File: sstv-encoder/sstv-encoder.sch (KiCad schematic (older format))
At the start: 18 parts, among them U1 ANTENNA_CONN, U2 LM386

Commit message: adding new things
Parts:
- added Alt1: AltlMU-10, sstv-encoder:AltIMU-10, symbol project-components:AltlMU-10
- added U3: Adafruit_GPS_MTK3339, sstv-encoder:Adafruit_GPS, symbol project-components:Adafruit_GPS_MTK3339
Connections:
- net +3V3: now also Alt1.5 (VIN), U3.8 (VIN)
- net GNDREF: now also Alt1.3 (GND), U3.7 (GND)
- net TX_GPS: now reaches DUE1.11 (RX3)
- net TX_GPS: now also U3.5 (TX)
- net RX_GPS: now reaches DUE1.12 (TX3)
- net RX_GPS: now also U3.6 (RX)
- net AF_APRS: now reaches DUE1.21 (D2)
- new net SCL_IMU: Alt1.1 (SCL)
- new net SDA_IMU: Alt1.2 (SDA)
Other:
- moved on the sheet: SIN1
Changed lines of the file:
@@
 L project-components:ADS9850 SIN1
 U 1 1 5E6BC8CF
-P 3200 4900
-F 0 "SIN1" H 3050 6515 50  0000 C CNN
-F 1 "ADS9850" H 3050 6424 50  0000 C CNN
-F 2 "sstv-encoder:AD9850" H 3050 4950 50  0001 C CNN
-F 3 "" H 3050 4950 50  0001 C CNN
-	1    3200 4900
-	1    0    0    -1
-$EndComp
-Wire Wire Line
-	2400 3650 1850 3650
-Wire Wire Line
-	1850 3650 1850 3300
+P 2800 5300
+F 0 "SIN1" H 2650 6915 50  0000 C CNN
+F 1 "ADS9850" H 2650 6824 50  0000 C CNN
+F 2 "sstv-encoder:AD9850" H 2650 5350 50  0001 C CNN
+F 3 "" H 2650 5350 50  0001 C CNN
+	1    2800 5300
+	1    0    0    -1
+$EndComp
+Wire Wire Line
+	2000 4050 1450 4050
+Wire Wire Line
+	1450 4050 1450 3700
 $Comp
 L power:+5V #PWR0113
 U 1 1 5E6ECCC4
-P 1850 3300
-F 0 "#PWR0113" H 1850 3150 50  0001 C CNN
-F 1 "+5V" H 1865 3473 50  0000 C CNN
-F 2 "" H 1850 3300 50  0001 C CNN
-F 3 "" H 1850 3300 50  0001 C CNN
-	1    1850 3300
-	1    0    0    -1
-$EndComp
-Wire Wire Line
-	2400 3750 1600 3750
-Wire Wire Line
-	2400 3850 1600 3850
-Wire Wire Line
-	2400 3950 1600 3950
-Wire Wire Line
-	2400 4050 1600 4050
-Wire Wire Line
-	2400 4150 1200 4150
-Wire Wire Line
-	1200 4150 1200 4500
+P 1450 3700
+F 0 "#PWR0113" H 1450 3550 50  0001 C CNN
+F 1 "+5V" H 1465 3873 50  0000 C CNN
+F 2 "" H 1450 3700 50  0001 C CNN
+F 3 "" H 1450 3700 50  0001 C CNN
+	1    1450 3700
+	1    0    0    -1
+$EndComp
+Wire Wire Line
+	2000 4150 1200 4150
+Wire Wire Line
+	2000 4250 1200 4250
+Wire Wire Line
+	2000 4350 1200 4350
+Wire Wire Line
+	2000 4450 1200 4450
+Wire Wire Line
+	2000 4550 800  4550
+Wire Wire Line
+	800  4550 800  4900
 $Comp
 L power:GNDREF #PWR0114
 U 1 1 5E6F3B16
-P 1200 4500
-F 0 "#PWR0114" H 1200 4250 50  0001 C CNN
-F 1 "GNDREF" H 1205 4327 50  0000 C CNN
-F 2 "" H 1200 4500 50  0001 C CNN
-F 3 "" H 1200 4500 50  0001 C CNN
-	1    1200 4500
-	1    0    0    -1
-$EndComp
-Wire Wire Line
-	2400 4550 1650 4550
-Wire Wire Line
-	3700 4550 4250 4550
-Wire Wire Line
-	4250 4550 4250 4950
+P 800 4900
+F 0 "#PWR0114" H 800 4650 50  0001 C CNN
+F 1 "GNDREF" H 805 4727 50  0000 C CNN
+F 2 "" H 800 4900 50  0001 C CNN
+F 3 "" H 800 4900 50  0001 C CNN
+	1    800  4900
+	1    0    0    -1
+$EndComp
+Wire Wire Line
+	2000 4950 1250 4950
+Wire Wire Line
+	3300 4950 3850 4950
+Wire Wire Line
+	3850 4950 3850 5350
 $Comp
 L power:GNDREF #PWR0115
 U 1 1 5E6F749A
-P 4250 4950
-F 0 "#PWR0115" H 4250 4700 50  0001 C CNN
-F 1 "GNDREF" H 4255 4777 50  0000 C CNN
-F 2 "" H 4250 4950 50  0001 C CNN
-F 3 "" H 4250 4950 50  0001 C CNN
-	1    4250 4950
-	1    0    0    -1
-$EndComp
-Text Label 1600 3750 0    50   ~ 0
+P 3850 5350
+F 0 "#PWR0115" H 3850 5100 50  0001 C CNN
+F 1 "GNDREF" H 3855 5177 50  0000 C CNN
+F 2 "" H 3850 5350 50  0001 C CNN
+F 3 "" H 3850 5350 50  0001 C CNN
+	1    3850 5350
+	1    0    0    -1
+$EndComp
+Text Label 1200 4150 0    50   ~ 0
 W_CLK_ADS
-Text Label 1600 3850 0    50   ~ 0
+Text Label 1200 4250 0    50   ~ 0
 FQ_UD_ADS
-Text Label 1600 3950 0    50   ~ 0
+Text Label 1200 4350 0    50   ~ 0
 DATA_ADS
-Text Label 1600 4050 0    50   ~ 0
+Text Label 1200 4450 0    50   ~ 0
 RESET_ADS
 Wire Wire Line
@@
 Text Label 4050 1750 0    50   ~ 0
 RESET_ADS
-Text Label 1650 4550 0    50   ~ 0
+Text Label 1250 4950 0    50   ~ 0
 ZOUT_ADS
 $Comp
@@
 Text Notes 7600 2300 0    50   ~ 0
 50 ohm
+$Comp
+L project-components:Adafruit_GPS_MTK3339 U3
+U 1 1 5E71EA4C
+P 5050 3600
+F 0 "U3" H 5025 4025 50  0000 C CNN
+F 1 "Adafruit_GPS_MTK3339" H 5025 3934 50  0000 C CNN
+F 2 "sstv-encoder:Adafruit_GPS" H 5000 3400 50  0001 C CNN
+F 3 "" H 5000 3400 50  0001 C CNN
+	1    5050 3600
+	1    0    0    -1
+$EndComp
+$Comp
+L project-components:AltlMU-10 Alt1
+U 1 1 5E71F53C
+P 5500 5200
+F 0 "Alt1" H 5475 5775 50  0000 C CNN
+F 1 "AltlMU-10" H 5475 5684 50  0000 C CNN
+F 2 "sstv-encoder:AltIMU-10" H 5500 5200 50  0001 C CNN
+F 3 "" H 5500 5200 50  0001 C CNN
+	1    5500 5200
+	1    0    0    -1
+$EndComp
+$Comp
+L power:GNDREF #PWR01
+U 1 1 5E720A54
+P 4050 4050
+F 0 "#PWR01" H 4050 3800 50  0001 C CNN
+F 1 "GNDREF" H 4055 3877 50  0000 C CNN
+F 2 "" H 4050 4050 50  0001 C CNN
+F 3 "" H 4050 4050 50  0001 C CNN
+	1    4050 4050
+	1    0    0    -1
+$EndComp
+$Comp
+L power:GNDREF #PWR02
+U 1 1 5E72154B
+P 4950 5250
+F 0 "#PWR02" H 4950 5000 50  0001 C CNN
+F 1 "GNDREF" H 4955 5077 50  0000 C CNN
+F 2 "" H 4950 5250 50  0001 C CNN
+F 3 "" H 4950 5250 50  0001 C CNN
+	1    4950 5250
+	1    0    0    -1
+$EndComp
+Wire Wire Line
+	6400 3800 5850 3800
+$Comp
+L power:+3.3V #PWR04
+U 1 1 5E72C5C7
+P 6550 4950
+F 0 "#PWR04" H 6550 4800 50  0001 C CNN
+F 1 "+3.3V" H 6565 5123 50  0000 C CNN
+F 2 "" H 6550 4950 50  0001 C CNN
+F 3 "" H 6550 4950 50  0001 C CNN
+	1    6550 4950
+	1    0    0    -1
+$EndComp
+Wire Wire Line
+	5850 4950 6550 4950
+Wire Wire Line
+	3350 2600 4050 2600
+Wire Wire Line
+	3350 2700 4050 2700
+Wire Wire Line
+	5100 5050 4950 5050
+Wire Wire Line
+	4950 5050 4950 5250
+Wire Wire Line
+	5100 4950 4750 4950
+Wire Wire Line
+	5100 4850 4750 4850
+Text Label 4750 4950 0    50   ~ 0
+SDA_IMU
+Text Label 4750 4850 0    50   ~ 0
+SCL_IMU
+Text Label 4050 2600 0    50   ~ 0
+SDA_IMU
+Text Label 4050 2700 0    50   ~ 0
+SCL_IMU
+Wire Wire Line
+	4050 4050 4050 3800
+Wire Wire Line
+	4050 3800 4200 3800
+Wire Wire Line
+	5850 3400 6400 3400
+Wire Wire Line
+	5850 3500 6400 3500
+Text Label 6400 3400 0    50   ~ 0
+TX_GPS
+Text Label 6400 3500 0    50   ~ 0
+RX_GPS
+Wire Wire Line
+	2300 2600 1700 2600
+Wire Wire Line
+	2300 2700 1700 2700
+Text Label 1700 2600 0    50   ~ 0
+TX_GPS
+Text Label 1700 2700 0    50   ~ 0
+RX_GPS
+$Comp
+L power:+3.3V #PWR03
+U 1 1 5E762D52
+P 6400 3800
+F 0 "#PWR03" H 6400 3650 50  0001 C CNN
+F 1 "+3.3V" H 6415 3973 50  0000 C CNN
+F 2 "" H 6400 3800 50  0001 C CNN
+F 3 "" H 6400 3800 50  0001 C CNN
+	1    6400 3800
+	1    0    0    -1
+$EndComp
+Wire Wire Line
+	3350 2350 4050 2350
+Text Label 4050 2350 0    50   ~ 0
+AF_APRS
 $EndSCHEMATC

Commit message: update sch
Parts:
- added C?: C, symbol Device:C
- added RV?: 10K, Potentiometer_SMD:Potentiometer_Bourns_3214J_Horizontal, symbol Device:R_POT
- added U?: TL082, symbol Amplifier_Operational:TL082
- added U?: 4053, symbol 4xxx:4053
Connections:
- net +5V: now also U?.16 (VDD)
- net AF_APRS: now also C?.2
- net GNDREF: now also RV?.3
- net SCL_IMU: now also DUE1.24 (SCL)
- net SDA_IMU: now also DUE1.23 (SDA)
- net ZOUT_ADS: now also U?.12 (X0); no longer R1.2
- net MUX_SL: now reaches DUE1.22 (D37)
- net MUX_SL: now also U?.11 (A)
- new net: C?.1, RV?.1
- new net: RV?.2, U?.3 (+)
- new net AF_APRS_NORM: U?.1, U?.13 (X1), U?.2 (-)
- new net AF_MUX: R1.2, U?.14 (X)
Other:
- note added: "ANALOG SIGNAL MULTIPLEXOR"
- note added: "AUDIO AMPLIFIER"
- note added: "PWN SIGNAL CORRECTION - APRS"
- moved on the sheet: C5, C7, R1, R2, RV1, U2

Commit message: update schematic
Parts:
- removed U?: 4053, symbol 4xxx:4053
- added C10, C11: 10uF, Capacitor_THT:CP_Radial_D5.0mm_P2.50mm, symbol Device:CP1
- added U5: DG419LDJ, Package_DIP:DIP-8_W7.62mm, symbol Analog_Switch:DG419LDJ
- added U6: LTC1044, Package_DIP:DIP-8_W7.62mm, symbol Regulator_SwitchedCapacitor:LTC1044
- C9: renamed from C?; value C -> 1uF; footprint (none) -> Capacitor_THT:CP_Radial_D5.0mm_P2.50mm
- RV1: footprint Potentiometer_SMD:Potentiometer_Bourns_3214J_Horizontal -> Potentiometer_THT:Potentiometer_Piher_PT-10-V10_Vertical
- RV2: renamed from RV?; footprint Potentiometer_SMD:Potentiometer_Bourns_3214J_Horizontal -> Potentiometer_THT:Potentiometer_Piher_PT-10-V10_Vertical
- U4: renamed from U?; footprint (none) -> Package_DIP:DIP-8-16_W7.62mm
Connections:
- net +3V3: now also U6.8 (V+); no longer U3.8 (VIN)
- net +5V: now also U3.8 (VIN)
- net AF_APRS: now also U5.2
- net AF_MUX: now also U5.1
- net GNDREF: now also C10.1, U6.3 (GND), U6.7 (OSC)
- net MUX_SL: now also U5.6
- net ZOUT_ADS: now also U5.8
- new net: C11.1, U6.2 (CAP+)
- new net: C11.2, U6.4 (CAP-)
- new net -VCC3.3: C10.2, U6.5 (VOUT)
- no-connect marks 0 -> 2
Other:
- note added: "DC-DC INVERTER"
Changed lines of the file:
@@
 F 0 "RV1" H 9381 8896 50  0000 R CNN
 F 1 "10K" H 9381 8805 50  0000 R CNN
-F 2 "Potentiometer_SMD:Potentiometer_Bourns_3214J_Horizontal" H 9450 8850 50  0001 C CNN
+F 2 "Potentiometer_THT:Potentiometer_Piher_PT-10-V10_Vertical" H 9450 8850 50  0001 C CNN
 F 3 "~" H 9450 8850 50  0001 C CNN
 	1    9450 8850
@@
 	1    0    0    -1
 $EndComp
-Text Notes 7600 2300 0    50   ~ 0
+Text Notes 7750 2300 0    50   ~ 0
 50 ohm
 $Comp
@@
 Text Label 1700 2700 0    50   ~ 0
 RX_GPS
-$Comp
-L power:+3.3V #PWR03
-U 1 1 5E762D52
-P 6400 3800
-F 0 "#PWR03" H 6400 3650 50  0001 C CNN
-F 1 "+3.3V" H 6415 3973 50  0000 C CNN
-F 2 "" H 6400 3800 50  0001 C CNN
-F 3 "" H 6400 3800 50  0001 C CNN
-	1    6400 3800
-	1    0    0    -1
-$EndComp
 Wire Wire Line
 	3350 2350 4050 2350
@@
 PWN SIGNAL CORRECTION - APRS
 $Comp
-L Device:C C?
+L Device:C C9
 U 1 1 5E8B30D2
 P 1300 8850
-F 0 "C?" V 1048 8850 50  0000 C CNN
-F 1 "C" V 1139 8850 50  0000 C CNN
-F 2 "" H 1338 8700 50  0001 C CNN
+F 0 "C9" V 1048 8850 50  0000 C CNN
+F 1 "1uF" V 1139 8850 50  0000 C CNN
+F 2 "Capacitor_THT:CP_Radial_D5.0mm_P2.50mm" H 1338 8700 50  0001 C CNN
 F 3 "~" H 1300 8850 50  0001 C CNN
 	1    1300 8850
@@
 $EndComp
 $Comp
-L Amplifier_Operational:TL082 U?
+L Amplifier_Operational:TL082 U4
 U 1 1 5E8B35EC
 P 2600 8950
-F 0 "U?" H 2600 9317 50  0000 C CNN
+F 0 "U4" H 2600 9317 50  0000 C CNN
 F 1 "TL082" H 2600 9226 50  0000 C CNN
-F 2 "" H 2600 8950 50  0001 C CNN
+F 2 "Package_DIP:DIP-8-16_W7.62mm" H 2600 8950 50  0001 C CNN
 F 3 "http://www.ti.com/lit/ds/symlink/tl081.pdf" H 2600 8950 50  0001 C CNN
 	1    2600 8950
@@
 $EndComp
 $Comp
-L Device:R_POT RV?
+L Device:R_POT RV2
 U 1 1 5E8B8628
 P 1650 9150
-F 0 "RV?" H 1581 9196 50  0000 R CNN
+F 0 "RV2" H 1581 9196 50  0000 R CNN
 F 1 "10K" H 1581 9105 50  0000 R CNN
-F 2 "Potentiometer_SMD:Potentiometer_Bourns_3214J_Horizontal" H 1650 9150 50  0001 C CNN
+F 2 "Potentiometer_THT:Potentiometer_Piher_PT-10-V10_Vertical" H 1650 9150 50  0001 C CNN
 F 3 "~" H 1650 9150 50  0001 C CNN
 	1    1650 9150
@@
 	1650 8850 1450 8850
 $Comp
-L power:GNDREF #PWR?
+L power:GNDREF #PWR0124
 U 1 1 5E8EE923
 P 1650 9550
-F 0 "#PWR?" H 1650 9300 50  0001 C CNN
+F 0 "#PWR0124" H 1650 9300 50  0001 C CNN
 F 1 "GNDREF" H 1655 9377 50  0000 C CNN
 F 2 "" H 1650 9550 50  0001 C CNN
@@
 Text Label 950  8850 2    50   ~ 0
 AF_APRS
-Text Notes 4300 7800 0    50   ~ 0
+Text Notes 4650 8050 0    50   ~ 0
 ANALOG SIGNAL MULTIPLEXOR
-$Comp
-L 4xxx:4053 U?
-U 1 1 5E903E36
-P 6100 9150
-F 0 "U?" H 6100 9350 50  0000 C CNN
-F 1 "4053" H 6100 9250 50  0000 C CNN
-F 2 "" H 6100 9150 50  0001 C CNN
-F 3 "http://www.intersil.com/content/dam/Intersil/documents/cd40/cd4051bms-52bms-53bms.pdf" H 6100 9150 50  0001 C CNN
-	1    6100 9150
-	1    0    0    -1
-$EndComp
-Wire Wire Line
-	5600 8550 5450 8550
-Wire Wire Line
-	5450 8550 5450 8400
-Wire Wire Line
-	5450 8400 5150 8400
-Wire Wire Line
-	5600 8650 5450 8650
-Wire Wire Line
-	5450 8650 5450 8800
-Wire Wire Line
-	5450 8800 5150 8800
 Text Label 3500 8950 0    50   ~ 0
 AF_APRS_NORM
-Text Label 5150 8400 2    50   ~ 0
-ZOUT_ADS
-Text Label 5150 8800 2    50   ~ 0
-AF_APRS_NORM
-Wire Wire Line
-	6600 8550 7000 8550
-Text Label 7000 8550 0    50   ~ 0
-AF_MUX
 Wire Wire Line
 	3350 2750 4050 2750
 Wire Wire Line
 	3350 2850 4050 2850
-Wire Wire Line
-	5600 9550 5150 9550
-Text Label 5150 9550 2    50   ~ 0
-MUX_SL
 Wire Wire Line
 	3350 2550 4050 2550
@@
 AUDIO AMPLIFIER
 $Comp
+L Analog_Switch:DG419LDJ U5
+U 1 1 5E9644DF
+P 5850 8750
+F 0 "U5" H 5850 8992 50  0000 C CNN
+F 1 "DG419LDJ" H 5850 8901 50  0000 C CNN
+F 2 "Package_DIP:DIP-8_W7.62mm" H 5850 8450 50  0001 C CNN
+F 3 "https://datasheets.maximintegrated.com/en/ds/DG417-DG419.pdf" H 5850 8550 50  0001 C CNN
+	1    5850 8750
+	-1   0    0    -1
+$EndComp
+Wire Wire Line
+	6150 8850 6550 8850
+Wire Wire Line
+	5550 8750 5100 8750
+Wire Wire Line
+	5550 8950 5100 8950
+Text Label 5100 8750 2    50   ~ 0
+AF_APRS
+Text Label 5100 8950 2    50   ~ 0
+ZOUT_ADS
+Wire Wire Line
+	5850 9150 5850 9500
+Text Label 5850 9500 3    50   ~ 0
+MUX_SL
+Text Label 6550 8850 0    50   ~ 0
+AF_MUX
+Text Notes 9350 4100 0    50   ~ 0
+DC-DC INVERTER
+$Comp
+L Regulator_SwitchedCapacitor:LTC1044 U6
+U 1 1 5E99155A
+P 10300 5350
+F 0 "U6" H 10300 6000 50  0000 C CNN
+F 1 "LTC1044" H 10300 5900 50  0000 C CNN
+F 2 "Package_DIP:DIP-8_W7.62mm" H 10400 5250 50  0001 C CNN
+F 3 "https://www.analog.com/media/en/technical-documentation/data-sheets/lt1044.pdf" H 10400 5250 50  0001 C CNN
+	1    10300 5350
+	1    0    0    -1
+$EndComp
+$Comp
+L power:GNDREF #PWR0125
+U 1 1 5E992017
+P 10300 6200
+F 0 "#PWR0125" H 10300 5950 50  0001 C CNN
+F 1 "GNDREF" H 10305 6027 50  0000 C CNN
+F 2 "" H 10300 6200 50  0001 C CNN
+F 3 "" H 10300 6200 50  0001 C CNN
+	1    10300 6200
+	1    0    0    -1
+$EndComp
+Wire Wire Line
+	10950 5650 10700 5650
+Wire Wire Line
+	10700 5250 11400 5250
+Wire Wire Line
+	11400 5250 11400 5650
+Wire Wire Line
+	11400 5650 11250 5650
+Wire Wire Line
+	10300 5850 10300 6200
+NoConn ~ 9900 5150
+NoConn ~ 9900 5550
+Wire Wire Line
+	10700 5050 10950 5050
+Text Label 11700 5050 0    50   ~ 0
+-VCC3.3
+$Comp
+L power:GNDREF #PWR0126
+U 1 1 5E9D05D1
+P 9350 5450
+F 0 "#PWR0126" H 9350 5200 50  0001 C CNN
+F 1 "GNDREF" H 9355 5277 50  0000 C CNN
+F 2 "" H 9350 5450 50  0001 C CNN
+F 3 "" H 9350 5450 50  0001 C CNN
+	1    9350 5450
+	1    0    0    -1
+$EndComp
+Wire Wire Line
+	9350 5350 9350 5450
+Wire Wire Line
+	9350 5350 9900 5350
+$Comp
+L Device:CP1 C10
+U 1 1 5E9D6BC0
+P 9350 5200
+F 0 "C10" H 9235 5154 50  0000 R CNN
+F 1 "10uF" H 9235 5245 50  0000 R CNN
+F 2 "Capacitor_THT:CP_Radial_D5.0mm_P2.50mm" H 9350 5200 50  0001 C CNN
+F 3 "~" H 9350 5200 50  0001 C CNN
+	1    9350 5200
+	-1   0    0    1
+$EndComp
+Connection ~ 9350 5350
+Wire Wire Line
+	9350 5050 9350 4850
+Wire Wire Line
+	9350 4850 10950 4850
+Wire Wire Line
+	10950 4850 10950 5050
+Connection ~ 10950 5050
+Wire Wire Line
+	10950 5050 11700 5050
+$Comp
+L power:+3.3V #PWR0127
+U 1 1 5E9E3AE9
+P 9700 4750
+F 0 "#PWR0127" H 9700 4600 50  0001 C CNN
+F 1 "+3.3V" H 9715 4923 50  0000 C CNN
+F 2 "" H 9700 4750 50  0001 C CNN
+F 3 "" H 9700 4750 50  0001 C CNN
+	1    9700 4750
+	1    0    0    -1
+$EndComp
+Wire Wire Line
+	9700 4750 9700 5050
+Wire Wire Line
+	9700 5050 9900 5050
+$Comp
+L Device:CP1 C11
+U 1 1 5E9FBE03
+P 11100 5650
+F 0 "C11" V 10848 5650 50  0000 C CNN
+F 1 "10uF" V 10939 5650 50  0000 C CNN
+F 2 "Capacitor_THT:CP_Radial_D5.0mm_P2.50mm" H 11100 5650 50  0001 C CNN
+F 3 "~" H 11100 5650 50  0001 C CNN
+	1    11100 5650
+	0    1    1    0
+$EndComp
+$Comp
 L power:+5V #PWR?
-U 1 1 5E9732EE
-P 6100 7900
-F 0 "#PWR?" H 6100 7750 50  0001 C CNN
-F 1 "+5V" H 6115 8073 50  0000 C CNN
-F 2 "" H 6100 7900 50  0001 C CNN
-F 3 "" H 6100 7900 50  0001 C CNN
-	1    6100 7900
-	1    0    0    -1
-$EndComp
-Wire Wire Line
-	6100 7900 6100 8250
+U 1 1 5E9EEABC
+P 6400 3750
+F 0 "#PWR?" H 6400 3600 50  0001 C CNN
+F 1 "+5V" H 6415 3923 50  0000 C CNN
+F 2 "" H 6400 3750 50  0001 C CNN
+F 3 "" H 6400 3750 50  0001 C CNN
+	1    6400 3750
+	1    0    0    -1
+$EndComp
+Wire Wire Line
+	6400 3800 6400 3750
 $EndSCHEMATC

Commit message: finish pcb
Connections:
- no-connect marks 2 -> 28
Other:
- moved on the sheet: Alt1, C10, C11, CAM1, U3, U6

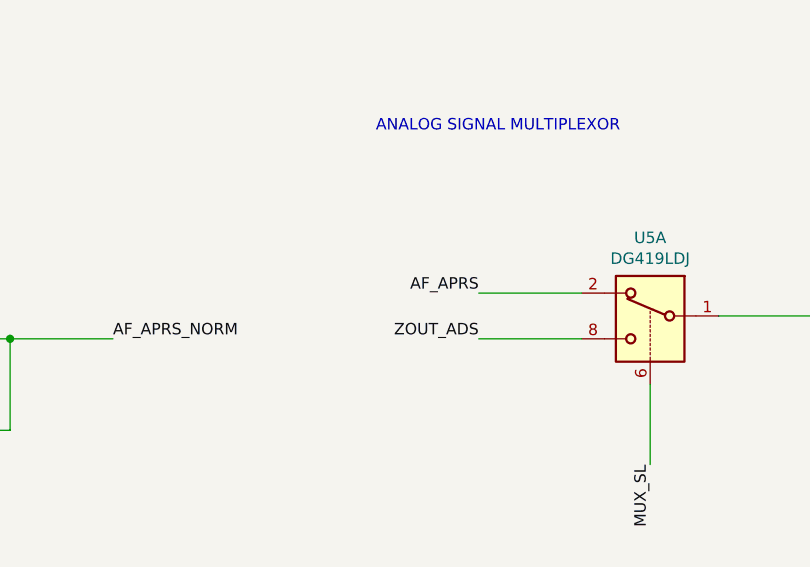
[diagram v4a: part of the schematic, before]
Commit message: fix footprint error
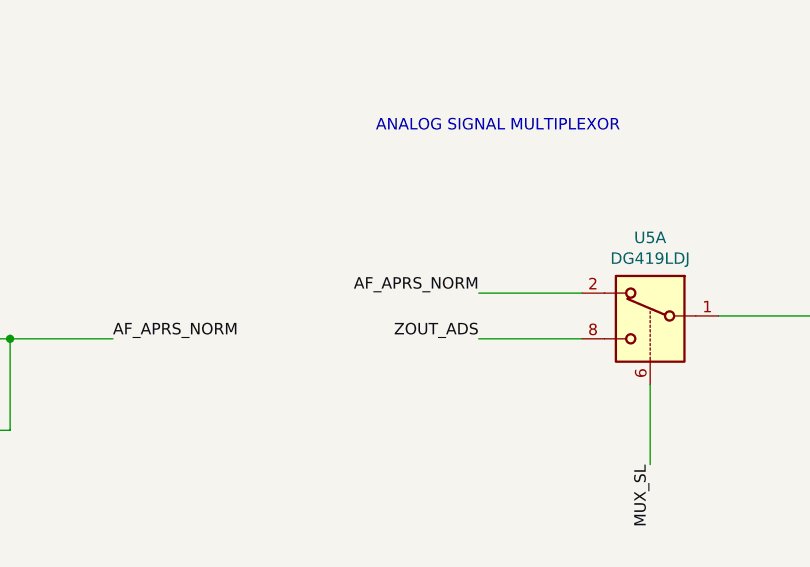
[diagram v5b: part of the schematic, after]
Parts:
- U4: footprint Package_DIP:DIP-8-16_W7.62mm -> Package_DIP:DIP-8_W7.62mm
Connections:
- net AF_APRS: no longer U5.2
- net AF_APRS_NORM: now also U5.2
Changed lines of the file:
@@
 F 0 "U4" H 2600 9317 50  0000 C CNN
 F 1 "TL082" H 2600 9226 50  0000 C CNN
-F 2 "Package_DIP:DIP-8-16_W7.62mm" H 2600 8950 50  0001 C CNN
+F 2 "Package_DIP:DIP-8_W7.62mm" H 2600 8950 50  0001 C CNN
 F 3 "http://www.ti.com/lit/ds/symlink/tl081.pdf" H 2600 8950 50  0001 C CNN
 	1    2600 8950
@@
 	5550 8950 5100 8950
 Text Label 5100 8750 2    50   ~ 0
-AF_APRS
+AF_APRS_NORM
 Text Label 5100 8950 2    50   ~ 0
 ZOUT_ADS
